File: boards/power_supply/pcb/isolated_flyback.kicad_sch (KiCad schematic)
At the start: 9 parts, among them U701 LM5181NGUR

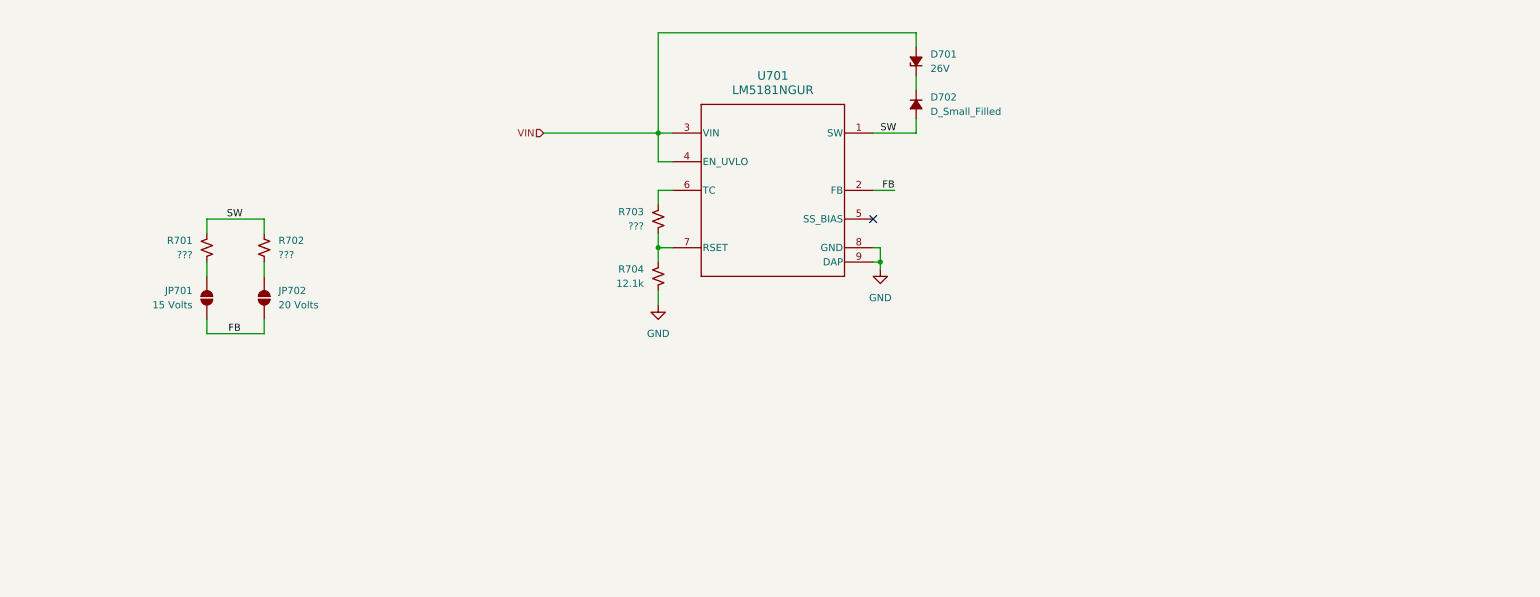
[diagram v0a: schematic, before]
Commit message: psu schematic capture
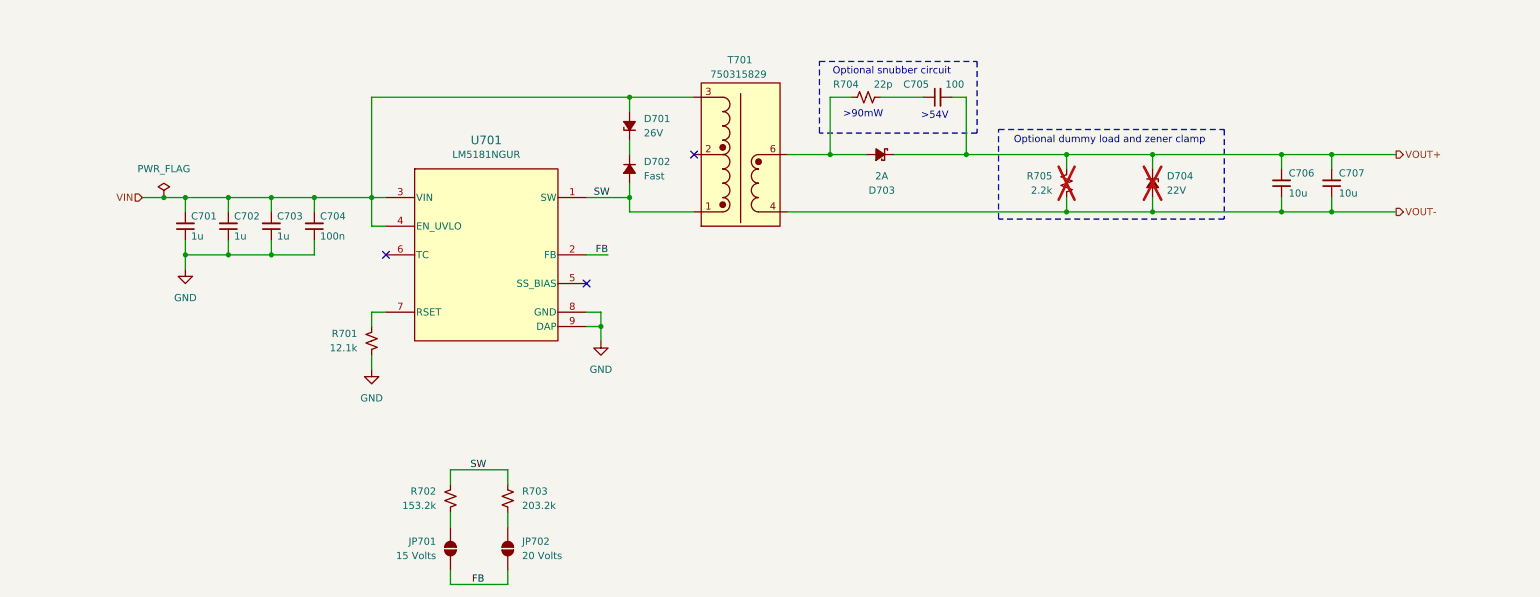
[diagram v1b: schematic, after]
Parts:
- removed R703: ???, symbol Device:R_Small_US
- added C701, C702, C703: 1u, symbol Device:C_Small
- added C704: 100n, symbol Device:C_Small
- added C705: 100, symbol Device:C_Small
- added C706, C707: 10u, symbol Device:C_Small
- added D703: 2A, symbol Device:D_Schottky_Small_Filled
- added D704: 22V, symbol Device:D_Zener_Small_Filled
- added R704: 22p, symbol Device:R_Small_US
- added R705: 2.2k, symbol Device:R_Small_US
- added T701: 150u, symbol 750315829:750315829
- D702: value D_Small_Filled -> Fast
- R702: renamed from R701; value ??? -> 153.2k
- R703: renamed from R702; value ??? -> 203.2k
- U701: value LM5181NGUR -> ~; MPN (none) -> LM5181NGUR
- renumbered R704 to R701
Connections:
- net GND: now also C701.1, C702.1, C703.1, C704.1
- net SW: now also T701.1
- net VIN: now also C701.2, C702.2, C703.2, C704.2, T701.3
- new net: D703.2 (A), R704.1, T701.6
- new net: C705.1, R704.2
- new net VOUT+: C705.2, C706.2, C707.2, D703.1 (K), D704.1 (K), R705.2
- new net VOUT-: C706.1, C707.1, D704.2 (A), R705.1, T701.4
- no-connect marks 1 -> 3
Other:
- note added: ">54V"
- note added: ">90mW"
- note added: "Optional dummy load and zener clamp"
- note added: "Optional snubber circuit"
- moved on the sheet: D701, D702, JP701, JP702, R701, R702, R703

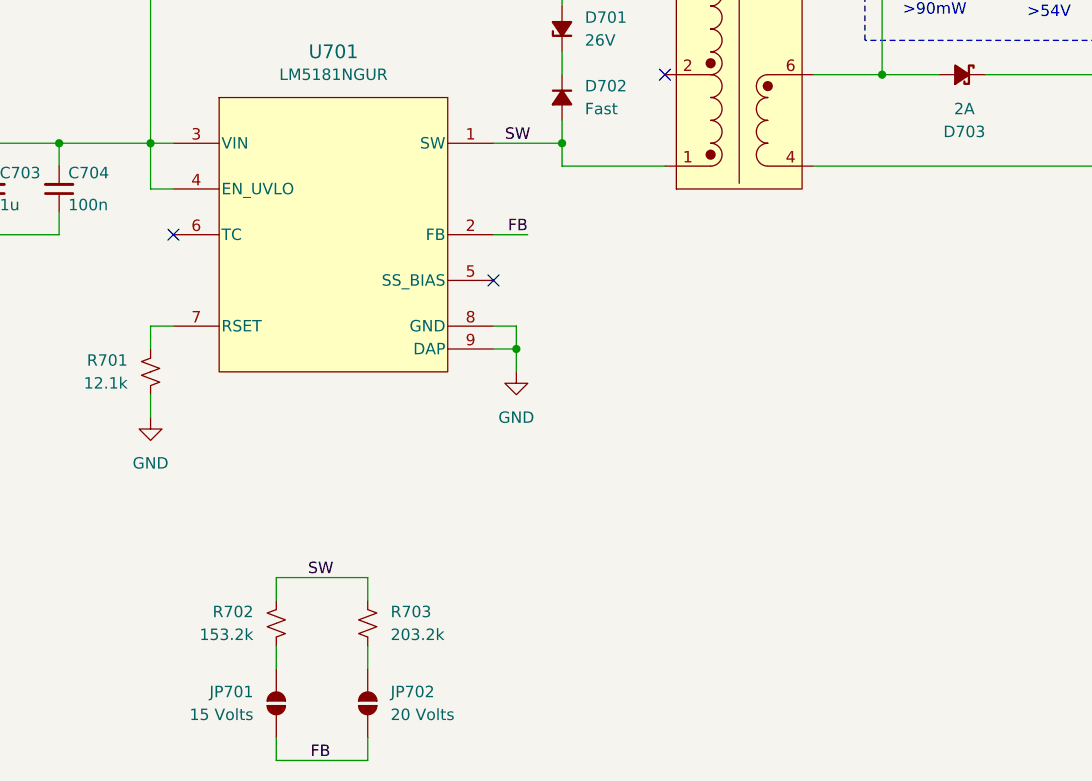
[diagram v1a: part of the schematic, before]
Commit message: psu component selection
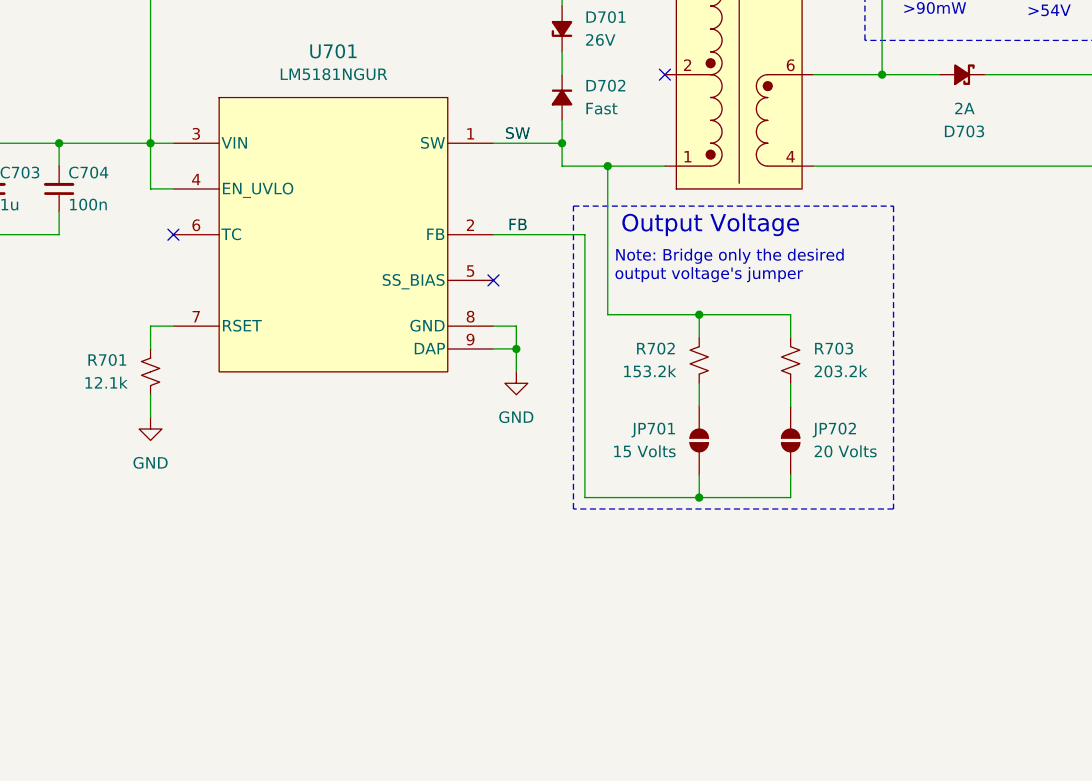
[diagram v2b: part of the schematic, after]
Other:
- note added: "Note: Bridge only the desired output voltage's jumper"
- note added: "Output Voltage"
- moved on the sheet: JP701, JP702, R702, R703
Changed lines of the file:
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@@
+	)
+	(junction
+		(at 137.16 132.08)
+		(diameter 0)
+		(color 0 0 0 0)
 	)
 	(junction
@@
 	(junction
 		(at 181.61 85.09)
+		(diameter 0)
+		(color 0 0 0 0)
+	)
+	(junction
+		(at 137.16 111.76)
+		(diameter 0)
+		(color 0 0 0 0)
+	)
+	(junction
+		(at 127 95.25)
 		(diameter 0)
 		(color 0 0 0 0)
@@
 	(wire
 		(pts
-			(xy 100.33 140.97) (xy 100.33 143.51)
-		)
-		(stroke
-			(width 0)
-			(type default)
-		)
-	)
-	(wire
-		(pts
-			(xy 118.11 102.87) (xy 114.3 102.87)
+			(xy 147.32 111.76) (xy 147.32 114.3)
 		)
 		(stroke
@@
 	(wire
 		(pts
-			(xy 90.17 158.75) (xy 90.17 161.29)
+			(xy 137.16 129.54) (xy 137.16 132.08)
 		)
 		(stroke
@@
 	(wire
 		(pts
-			(xy 90.17 143.51) (xy 90.17 140.97)
+			(xy 137.16 111.76) (xy 137.16 114.3)
 		)
 		(stroke
@@
 	(wire
 		(pts
-			(xy 100.33 148.59) (xy 100.33 151.13)
+			(xy 124.46 132.08) (xy 137.16 132.08)
+		)
+		(stroke
+			(width 0)
+			(type default)
+		)
+	)
+	(wire
+		(pts
+			(xy 147.32 119.38) (xy 147.32 121.92)
 		)
 		(stroke
@@
 	(wire
 		(pts
-			(xy 90.17 161.29) (xy 100.33 161.29)
+			(xy 137.16 132.08) (xy 147.32 132.08)
 		)
 		(stroke
@@
 	(wire
 		(pts
+			(xy 137.16 111.76) (xy 127 111.76)
+		)
+		(stroke
+			(width 0)
+			(type default)
+		)
+	)
+	(wire
+		(pts
 			(xy 58.42 92.71) (xy 58.42 95.25)
 		)
@@
 	(wire
 		(pts
+			(xy 124.46 102.87) (xy 114.3 102.87)
+		)
+		(stroke
+			(width 0)
+			(type default)
+		)
+	)
+	(wire
+		(pts
 			(xy 246.38 95.25) (xy 257.81 95.25)
 		)
@@
 	(wire
 		(pts
-			(xy 100.33 158.75) (xy 100.33 161.29)
+			(xy 147.32 129.54) (xy 147.32 132.08)
+		)
+		(stroke
+			(width 0)
+			(type default)
+		)
+	)
+	(wire
+		(pts
+			(xy 127 95.25) (xy 133.35 95.25)
+		)
+		(stroke
+			(width 0)
+			(type default)
+		)
+	)
+	(wire
+		(pts
+			(xy 124.46 102.87) (xy 124.46 132.08)
 		)
 		(stroke
@@
 	(wire
 		(pts
-			(xy 90.17 140.97) (xy 100.33 140.97)
-		)
-		(stroke
-			(width 0)
-			(type default)
-		)
-	)
-	(wire
-		(pts
-			(xy 90.17 148.59) (xy 90.17 151.13)
+			(xy 137.16 111.76) (xy 147.32 111.76)
+		)
+		(stroke
+			(width 0)
+			(type default)
+		)
+	)
+	(wire
+		(pts
+			(xy 137.16 119.38) (xy 137.16 121.92)
 		)
 		(stroke
@@
 	(wire
 		(pts
+			(xy 127 111.76) (xy 127 95.25)
+		)
+		(stroke
+			(width 0)
+			(type default)
+		)
+	)
+	(wire
+		(pts
 			(xy 50.8 92.71) (xy 58.42 92.71)
 		)
@@
 	(wire
 		(pts
-			(xy 121.92 95.25) (xy 133.35 95.25)
+			(xy 121.92 95.25) (xy 127 95.25)
 		)
 		(stroke
@@
 			(width 0)
 			(type default)
+		)
+	)
+	(rectangle
+		(start 123.19 99.695)
+		(end 158.75 133.35)
+		(stroke
+			(width 0)
+			(type dash)
+		)
+		(fill
+			(type none)
 		)
 	)
@@
 		)
 	)
+	(text "Note: Bridge only the desired \noutput voltage's jumper"
+		(exclude_from_sim no)
+		(at 127.762 106.426 0)
+		(effects
+			(font
+				(size 1.27 1.27)
+			)
+			(justify left)
+		)
+	)
 	(text "Optional snubber circuit"
 		(exclude_from_sim no)
@@
 		)
 	)
+	(text "Output Voltage"
+		(exclude_from_sim no)
+		(at 138.43 101.854 0)
+		(effects
+			(font
+				(size 1.905 1.905)
+			)
+		)
+	)
 	(label "FB"
 		(at 118.11 102.87 180)
@@
 			)
 			(justify right bottom)
-		)
-	)
-	(label "SW"
-		(at 96.52 140.97 180)
-		(fields_autoplaced yes)
-		(effects
-			(font
-				(size 1.27 1.27)
-			)
-			(justify right bottom)
-		)
-	)
-	(label "FB"
-		(at 93.98 161.29 0)
-		(fields_autoplaced yes)
-		(effects
-			(font
-				(size 1.27 1.27)
-			)
-			(justify left bottom)
 		)
 	)
@@
 	(symbol
 		(lib_id "Device:R_Small_US")
-		(at 90.17 146.05 0)
+		(at 137.16 116.84 0)
 		(mirror y)
 		(unit 1)
@@
 		(dnp no)
 		(property "Reference" "R702"
-			(at 87.63 144.7799 0)
+			(at 134.62 115.5699 0)
 			(effects
 				(font
@@
 		)
 		(property "Value" "153.2k"
-			(at 87.63 147.3199 0)
+			(at 134.62 118.1099 0)
 			(effects
 				(font
@@
 		)
 		(property "Footprint" ""
-			(at 90.17 146.05 0)
+			(at 137.16 116.84 0)
 			(effects
 				(font
@@
 		)
 		(property "Datasheet" "~"
-			(at 90.17 146.05 0)
+			(at 137.16 116.84 0)
 			(effects
 				(font
@@
 		)
 		(property "Description" "Resistor, small US symbol"
-			(at 90.17 146.05 0)
+			(at 137.16 116.84 0)
 			(effects
 				(font
@@
 	(symbol
 		(lib_id "Device:R_Small_US")
-		(at 100.33 146.05 0)
+		(at 147.32 116.84 0)
 		(unit 1)
 		(exclude_from_sim no)
@@
 		(fields_autoplaced yes)
 		(property "Reference" "R703"
-			(at 102.87 144.7799 0)
+			(at 149.86 115.5699 0)
 			(effects
 				(font
@@
 		)
 		(property "Value" "203.2k"
-			(at 102.87 147.3199 0)
+			(at 149.86 118.1099 0)
 			(effects
 				(font
@@
 		)
 		(property "Footprint" ""
-			(at 100.33 146.05 0)
+			(at 147.32 116.84 0)
 			(effects
 				(font
@@
 		)
 		(property "Datasheet" "~"
-			(at 100.33 146.05 0)
+			(at 147.32 116.84 0)
 			(effects
 				(font
@@
 		)
 		(property "Description" "Resistor, small US symbol"
-			(at 100.33 146.05 0)
+			(at 147.32 116.84 0)
 			(effects
 				(font
@@
 	(symbol
 		(lib_id "Jumper:SolderJumper_2_Open")
-		(at 90.17 154.94 270)
+		(at 137.16 125.73 270)
 		(mirror x)
 		(unit 1)
@@
 		(dnp no)
 		(property "Reference" "JP701"
-			(at 87.63 153.6699 90)
+			(at 134.62 124.4599 90)
 			(effects
 				(font
@@
 		)
 		(property "Value" "15 Volts"
-			(at 87.63 156.2099 90)
+			(at 134.62 126.9999 90)
 			(effects
 				(font
@@
 		)
 		(property "Footprint" ""
-			(at 90.17 154.94 0)
+			(at 137.16 125.73 0)
 			(effects
 				(font
@@
 		)
 		(property "Datasheet" "~"
-			(at 90.17 154.94 0)
+			(at 137.16 125.73 0)
 			(effects
 				(font
@@
 		)
 		(property "Description" "Solder Jumper, 2-pole, open"
-			(at 90.17 154.94 0)
+			(at 137.16 125.73 0)
 			(effects
 				(font
@@
 	(symbol
 		(lib_id "Jumper:SolderJumper_2_Open")
-		(at 100.33 154.94 90)
+		(at 147.32 125.73 90)
 		(unit 1)
 		(exclude_from_sim yes)
@@
 		(fields_autoplaced yes)
 		(property "Reference" "JP702"
-			(at 102.87 153.6699 90)
+			(at 149.86 124.4599 90)
 			(effects
 				(font
@@
 		)
 		(property "Value" "20 Volts"
-			(at 102.87 156.2099 90)
+			(at 149.86 126.9999 90)
 			(effects
 				(font
@@
 		)
 		(property "Footprint" ""
-			(at 100.33 154.94 0)
+			(at 147.32 125.73 0)
 			(effects
 				(font
@@
 		)
 		(property "Datasheet" "~"
-			(at 100.33 154.94 0)
+			(at 147.32 125.73 0)
 			(effects
 				(font
@@
 		)
 		(property "Description" "Solder Jumper, 2-pole, open"
-			(at 100.33 154.94 0)
-			(effects
-				(font
+			(at 147.32 125.73 0)
+			(effects
+				(font

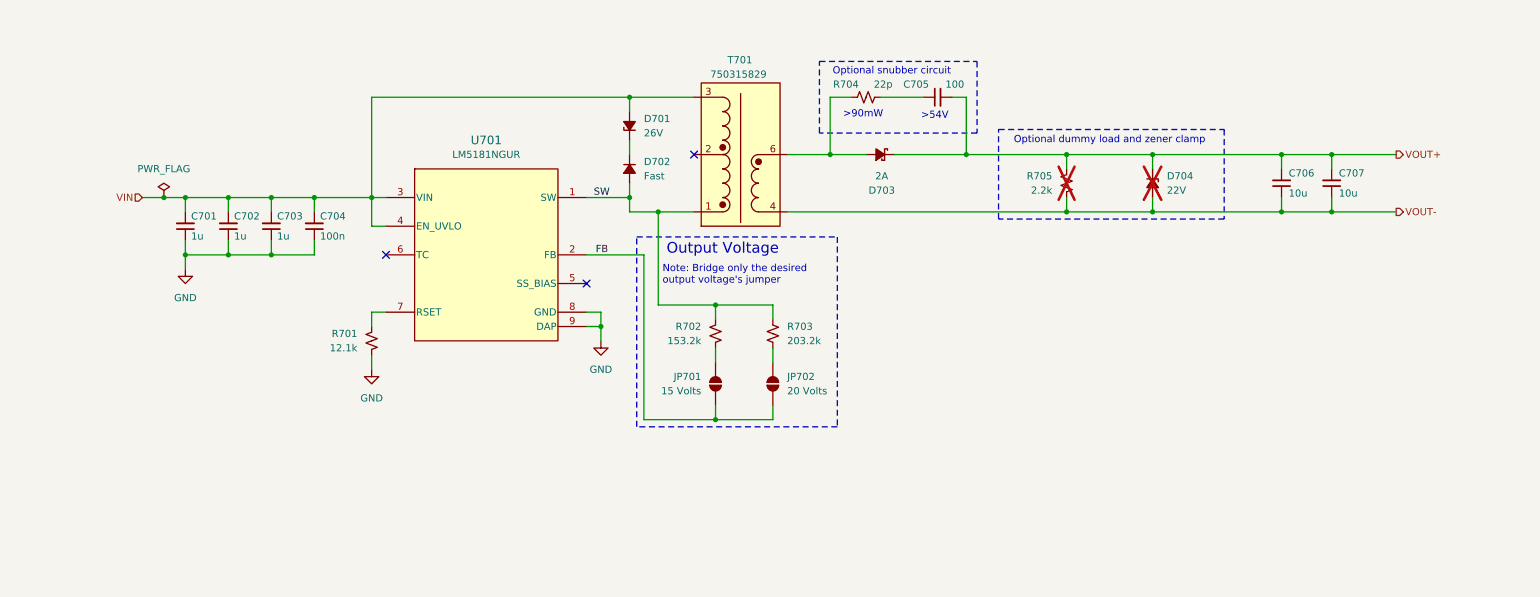
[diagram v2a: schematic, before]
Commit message: created psu footprints
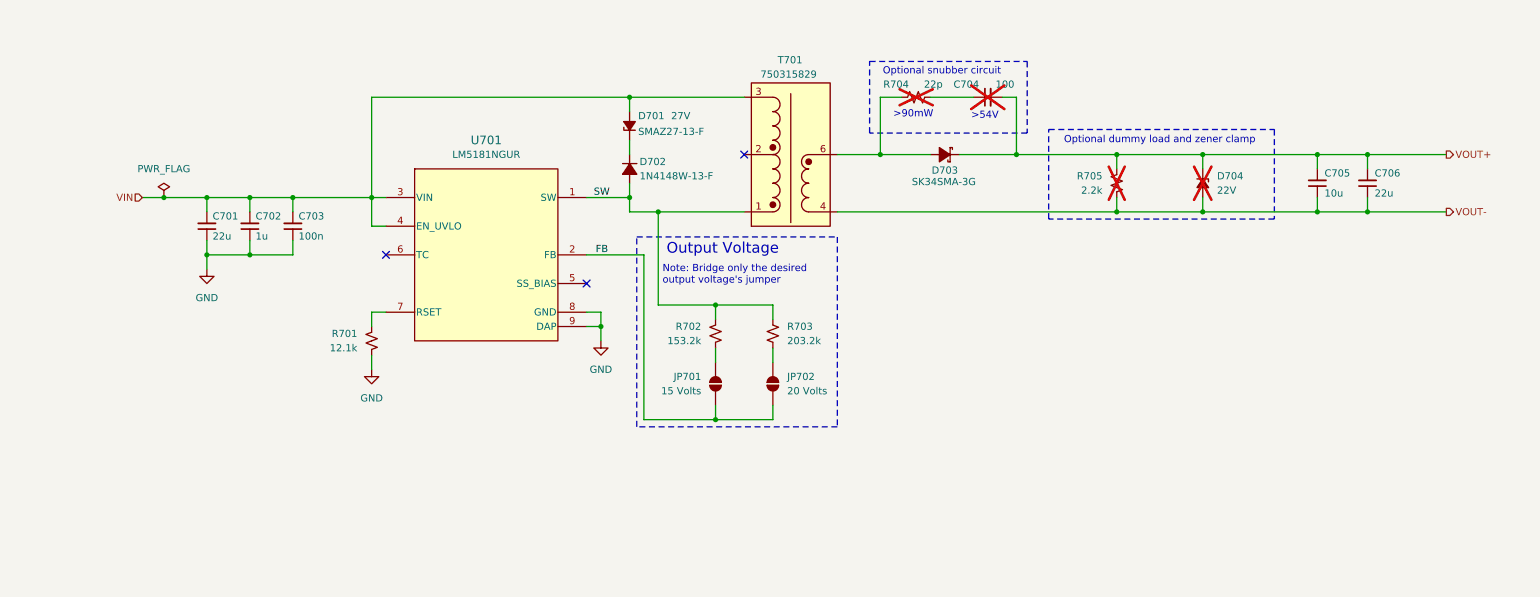
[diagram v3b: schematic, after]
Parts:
- removed C701: 1u, symbol Device:C_Small
- removed D701: 26V, symbol Device:D_Zener_Small_Filled
- removed D702: Fast, symbol Device:D_Small_Filled
- removed D703: 2A, symbol Device:D_Schottky_Small_Filled
- added D701: 27V, symbol SMAZ27-13-F:SMAZ27-13-F
- added D702: ~, 1N4148W-13-F:1N4148W-13-F, symbol 1N4148W-13-F:1N4148W-13-F
- added D703: ~, SK34SMA-3G:SK34SMA-3G, symbol SK34SMA-3G:SK34SMA-3G
- C701: renamed from C702; value 1u -> 22u
- C704: renamed from C705; now not fitted
- C706: value 10u -> 22u
- R704: now not fitted
- renumbered C703 to C702, C704 to C703, C707 to C705
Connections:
- net SW: now also D702.2
- net VIN: now also D701.2 (A)
- net VOUT+: now also D703.1
- net at R704.1, T701.6: now also D703.2
- new net: D701.1 (K), D702.1
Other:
- moved on the sheet: C701, C702, C703, C705, C706, D704, R705, T701

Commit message: starting psu layout
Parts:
- removed D704: 22V, symbol Device:D_Zener_Small_Filled
- added D704: 22V, SMAZ22-13-F:SMAZ22-13-F, symbol SMAZ22-13-F:SMAZ22-13-F
- C701, C706: footprint (none) -> Capacitor_SMD:C_1206_3216Metric
- C702, C703: footprint (none) -> Capacitor_SMD:C_0603_1608Metric
- C704: value 100 -> 22p; footprint (none) -> Capacitor_SMD:C_0603_1608Metric
- C705: footprint (none) -> Capacitor_SMD:C_0805_2012Metric
- D701: footprint (none) -> SMAZ27-13-F:SMAZ27-13-F
- JP701, JP702: footprint (none) -> Jumper:SolderJumper-2_P1.3mm_Open_RoundedPad1.0x1.5mm
- R701, R702, R703, R705: footprint (none) -> Resistor_SMD:R_0603_1608Metric
- R704: value 22p -> 100; footprint (none) -> Resistor_SMD:R_0603_1608Metric
- T701: footprint (none) -> 750315829:750315829
- U701: footprint NGU0008C-IPC_A -> LM5181NGUR:NGU0008C-IPC_A
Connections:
- net VOUT+: now also D704.1 (K)
- net VOUT-: now also D704.2 (A)
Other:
- note added: "Isolated Flyback Converter"
- moved on the sheet: C705, C706
